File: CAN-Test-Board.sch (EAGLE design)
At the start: 47 parts, among them Y1 ECS-80-S-4X, Y2 ECS-80-S-4X

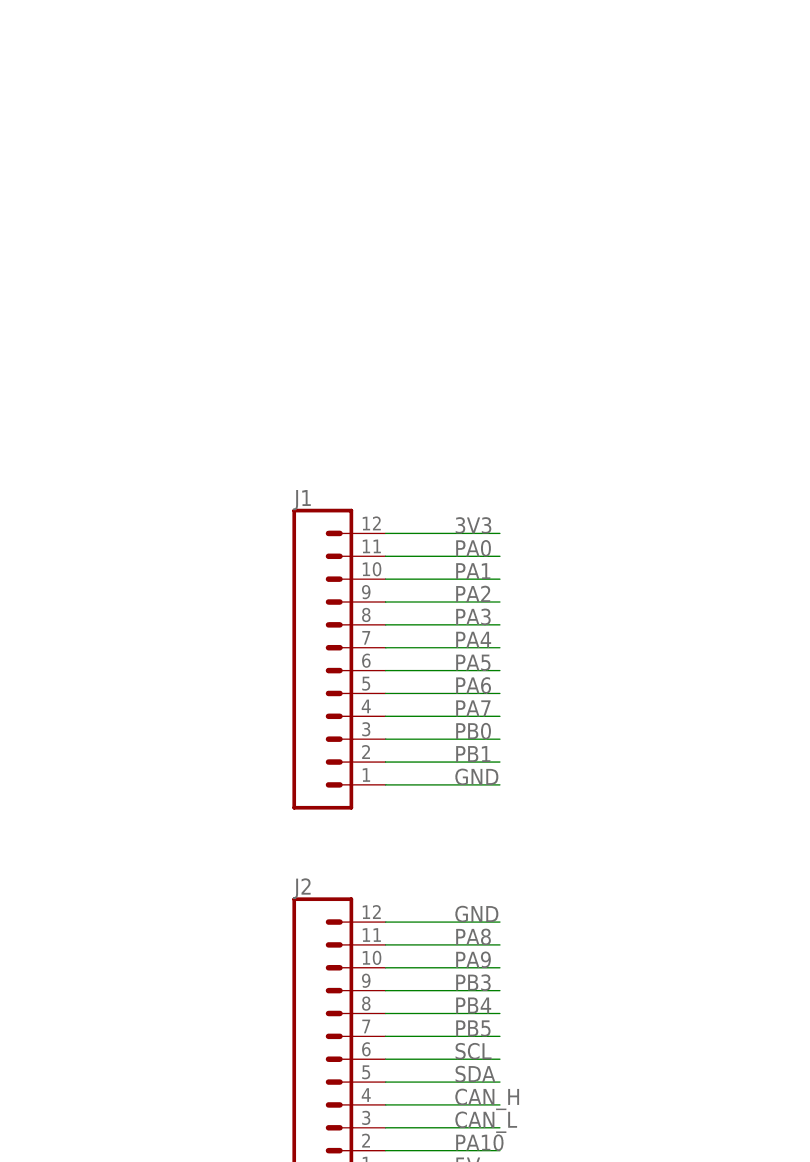
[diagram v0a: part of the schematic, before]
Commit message: smaller and extra CAN breakouts
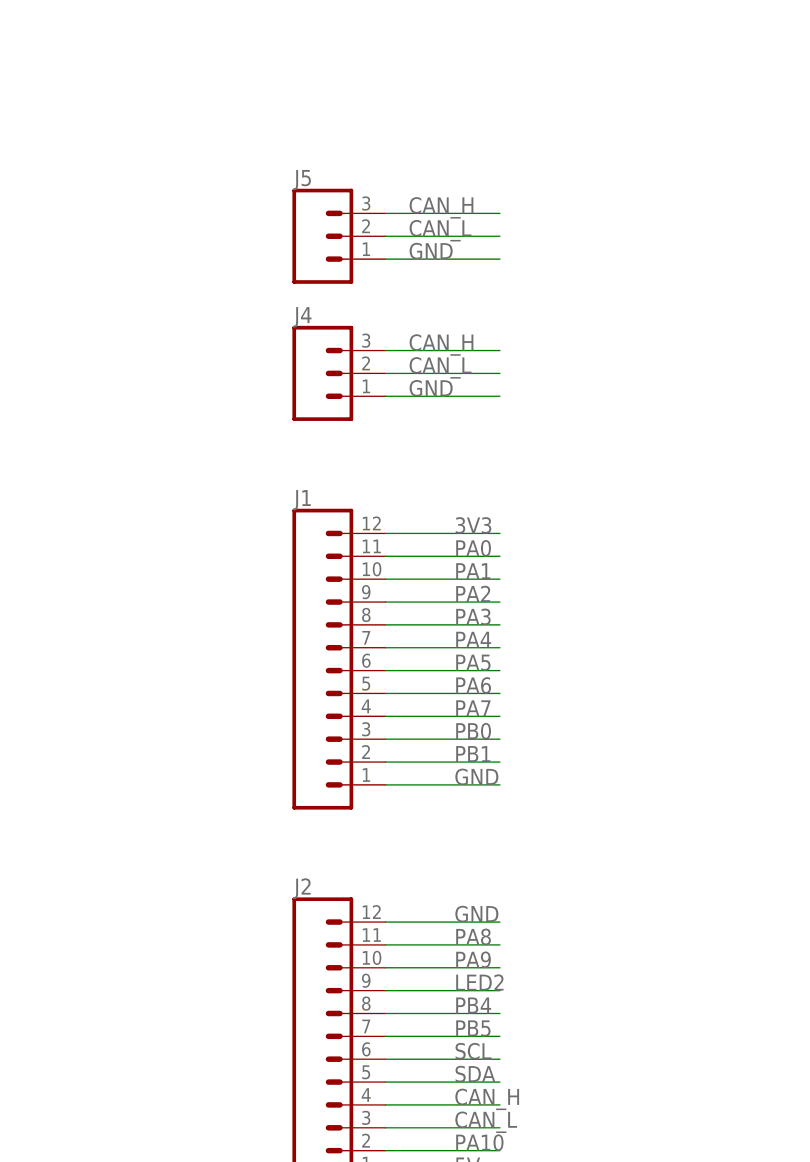
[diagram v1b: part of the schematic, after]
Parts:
- added J4, J5: (no value), SparkFun-Connectors:CONN_03
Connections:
- removed net PB3: J2.9
- net CAN_H: now also J4.3, J5.3
- net CAN_L: now also J4.2, J5.2
- net GND: now also J4.1, J5.1
- net LED2: now also J2.9
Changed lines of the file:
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@@
 <part name="R12" library="SparkFun-Resistors" library_urn="urn:adsk.eagle:library:532" deviceset="1KOHM" device="-0603-1/10W-1%" package3d_urn="urn:adsk.eagle:package:39650/1" value="10k"/>
 <part name="R13" library="SparkFun-Resistors" library_urn="urn:adsk.eagle:library:532" deviceset="1KOHM" device="-0603-1/10W-1%" package3d_urn="urn:adsk.eagle:package:39650/1" value="10k"/>
+<part name="J4" library="SparkFun-Connectors" library_urn="urn:adsk.eagle:library:513" deviceset="CONN_03" device="" package3d_urn="urn:adsk.eagle:package:38063/1"/>
+<part name="J5" library="SparkFun-Connectors" library_urn="urn:adsk.eagle:library:513" deviceset="CONN_03" device="" package3d_urn="urn:adsk.eagle:package:38063/1"/>
 </parts>
 <sheets>
@@
 <attribute name="NAME" x="135.636" y="165.1" size="1.778" layer="95" font="vector" rot="R90" align="bottom-center"/>
 <attribute name="VALUE" x="138.684" y="165.1" size="1.778" layer="96" font="vector" rot="R90" align="top-center"/>
+</instance>
+<instance part="J4" gate="J$1" x="307.34" y="116.84" smashed="yes">
+<attribute name="VALUE" x="304.8" y="109.474" size="1.778" layer="96" font="vector"/>
+<attribute name="NAME" x="304.8" y="122.428" size="1.778" layer="95" font="vector"/>
+</instance>
+<instance part="J5" gate="J$1" x="307.34" y="132.08" smashed="yes">
+<attribute name="VALUE" x="304.8" y="124.714" size="1.778" layer="96" font="vector"/>
+<attribute name="NAME" x="304.8" y="137.668" size="1.778" layer="95" font="vector"/>
 </instance>
 </instances>
@@
 <label x="322.58" y="55.88" size="1.778" layer="95"/>
 </segment>
+<segment>
+<pinref part="J4" gate="J$1" pin="1"/>
+<wire x1="314.96" y1="114.3" x2="327.66" y2="114.3" width="0.1524" layer="91"/>
+<label x="317.5" y="114.3" size="1.778" layer="95" rot="MR0" align="bottom-right"/>
+</segment>
+<segment>
+<pinref part="J5" gate="J$1" pin="1"/>
+<wire x1="314.96" y1="129.54" x2="327.66" y2="129.54" width="0.1524" layer="91"/>
+<label x="317.5" y="129.54" size="1.778" layer="95" rot="MR0" align="bottom-right"/>
+</segment>
 </net>
 <net name="CAN_H" class="1">
@@
 <pinref part="J2" gate="G$1" pin="4"/>
 <label x="322.58" y="35.56" size="1.778" layer="95"/>
+</segment>
+<segment>
+<pinref part="J4" gate="J$1" pin="3"/>
+<wire x1="314.96" y1="119.38" x2="327.66" y2="119.38" width="0.1524" layer="91"/>
+<label x="317.5" y="119.38" size="1.778" layer="95" rot="MR0" align="bottom-right"/>
+</segment>
+<segment>
+<pinref part="J5" gate="J$1" pin="3"/>
+<wire x1="314.96" y1="134.62" x2="327.66" y2="134.62" width="0.1524" layer="91"/>
+<label x="317.5" y="134.62" size="1.778" layer="95" rot="MR0" align="bottom-right"/>
 </segment>
 </net>
@@
 <pinref part="J2" gate="G$1" pin="3"/>
 <label x="322.58" y="33.02" size="1.778" layer="95"/>
+</segment>
+<segment>
+<pinref part="J4" gate="J$1" pin="2"/>
+<wire x1="314.96" y1="116.84" x2="327.66" y2="116.84" width="0.1524" layer="91"/>
+<label x="317.5" y="116.84" size="1.778" layer="95" rot="MR0" align="bottom-right"/>
+</segment>
+<segment>
+<pinref part="J5" gate="J$1" pin="2"/>
+<wire x1="314.96" y1="132.08" x2="327.66" y2="132.08" width="0.1524" layer="91"/>
+<label x="317.5" y="132.08" size="1.778" layer="95" rot="MR0" align="bottom-right"/>
 </segment>
 </net>
@@
 <label x="190.5" y="157.48" size="1.778" layer="95" rot="R90"/>
 </segment>
+<segment>
+<wire x1="314.96" y1="48.26" x2="327.66" y2="48.26" width="0.1524" layer="91"/>
+<pinref part="J2" gate="G$1" pin="9"/>
+<label x="322.58" y="48.26" size="1.778" layer="95"/>
+</segment>
 </net>
 <net name="SCLK" class="0">
@@
 <wire x1="157.48" y1="243.84" x2="139.7" y2="243.84" width="0.1524" layer="91"/>
 <label x="139.7" y="243.84" size="1.778" layer="95"/>
-</segment>
-</net>
-<net name="PB3" class="0">
-<segment>
-<wire x1="314.96" y1="48.26" x2="327.66" y2="48.26" width="0.1524" layer="91"/>
-<pinref part="J2" gate="G$1" pin="9"/>
-<label x="322.58" y="48.26" size="1.778" layer="95"/>
 </segment>
 </net>
@@
 packages will not be understood (or retained) with this version.
 </note>
+<note version="9.0" severity="warning">
+Since Version 9.0, EAGLE supports the align property for labels.
+Labels in schematic will not be understood with this version. Update EAGLE to the latest version
+for full support of labels.
+</note>
 <note version="8.5" severity="warning">

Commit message: labels and 3v3 power options
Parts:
- added R14: (no value), SparkFun-Resistors:RESISTOR0603
- added R15: 0, SparkFun-Resistors:RESISTOR0603
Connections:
- new net 3V3_PI: PCB1.3V3@1, PCB1.3V3@17, R15.1
- new net 3V3_REG: C17.1, R14.2, U$5.OUT
- net 3V3: now also R14.1, R15.2; no longer C17.1, U$5.OUT
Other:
- moved on the sheet: C17, C18
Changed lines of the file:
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@@
 <part name="J4" library="SparkFun-Connectors" library_urn="urn:adsk.eagle:library:513" deviceset="CONN_03" device="" package3d_urn="urn:adsk.eagle:package:38063/1"/>
 <part name="J5" library="SparkFun-Connectors" library_urn="urn:adsk.eagle:library:513" deviceset="CONN_03" device="" package3d_urn="urn:adsk.eagle:package:38063/1"/>
+<part name="R14" library="SparkFun-Resistors" library_urn="urn:adsk.eagle:library:532" deviceset="RESISTOR" device="0603" package3d_urn="urn:adsk.eagle:package:39650/1" value=" "/>
+<part name="R15" library="SparkFun-Resistors" library_urn="urn:adsk.eagle:library:532" deviceset="RESISTOR" device="0603" package3d_urn="urn:adsk.eagle:package:39650/1" value="0"/>
 </parts>
 <sheets>
@@
 <attribute name="SHEET" x="195.58" y="189.23" size="2.54" layer="94" font="vector"/>
 </instance>
-<instance part="U$5" gate="G$1" x="515.62" y="55.88" smashed="yes"/>
-<instance part="GND20" gate="1" x="523.24" y="35.56" smashed="yes">
-<attribute name="VALUE" x="523.24" y="35.306" size="1.778" layer="96" align="top-center"/>
-</instance>
-<instance part="C17" gate="G$1" x="538.48" y="43.18" smashed="yes">
-<attribute name="NAME" x="540.004" y="46.101" size="1.778" layer="95" font="vector"/>
-<attribute name="VALUE" x="540.004" y="41.021" size="1.778" layer="96" font="vector"/>
-</instance>
-<instance part="C18" gate="G$1" x="502.92" y="43.18" smashed="yes">
-<attribute name="NAME" x="504.444" y="46.101" size="1.778" layer="95" font="vector"/>
-<attribute name="VALUE" x="504.444" y="41.021" size="1.778" layer="96" font="vector"/>
-</instance>
-<instance part="GND21" gate="1" x="538.48" y="35.56" smashed="yes">
-<attribute name="VALUE" x="538.48" y="35.306" size="1.778" layer="96" align="top-center"/>
-</instance>
-<instance part="GND22" gate="1" x="502.92" y="35.56" smashed="yes">
-<attribute name="VALUE" x="502.92" y="35.306" size="1.778" layer="96" align="top-center"/>
+<instance part="U$5" gate="G$1" x="492.76" y="60.96" smashed="yes"/>
+<instance part="GND20" gate="1" x="500.38" y="40.64" smashed="yes">
+<attribute name="VALUE" x="500.38" y="40.386" size="1.778" layer="96" align="top-center"/>
+</instance>
+<instance part="C17" gate="G$1" x="515.62" y="48.26" smashed="yes">
+<attribute name="NAME" x="517.144" y="51.181" size="1.778" layer="95" font="vector"/>
+<attribute name="VALUE" x="517.144" y="46.101" size="1.778" layer="96" font="vector"/>
+</instance>
+<instance part="C18" gate="G$1" x="480.06" y="48.26" smashed="yes">
+<attribute name="NAME" x="481.584" y="51.181" size="1.778" layer="95" font="vector"/>
+<attribute name="VALUE" x="481.584" y="46.101" size="1.778" layer="96" font="vector"/>
+</instance>
+<instance part="GND21" gate="1" x="515.62" y="40.64" smashed="yes">
+<attribute name="VALUE" x="515.62" y="40.386" size="1.778" layer="96" align="top-center"/>
+</instance>
+<instance part="GND22" gate="1" x="480.06" y="40.64" smashed="yes">
+<attribute name="VALUE" x="480.06" y="40.386" size="1.778" layer="96" align="top-center"/>
 </instance>
 <instance part="D2" gate="G$1" x="220.98" y="35.56" smashed="yes">
@@
 <attribute name="VALUE" x="304.8" y="124.714" size="1.778" layer="96" font="vector"/>
 <attribute name="NAME" x="304.8" y="137.668" size="1.778" layer="95" font="vector"/>
+</instance>
+<instance part="R14" gate="G$1" x="525.78" y="55.88" smashed="yes" rot="R180">
+<attribute name="NAME" x="525.78" y="54.356" size="1.778" layer="95" font="vector" rot="R180" align="bottom-center"/>
+<attribute name="VALUE" x="525.78" y="57.404" size="1.778" layer="96" font="vector" rot="R180" align="top-center"/>
+</instance>
+<instance part="R15" gate="G$1" x="147.32" y="205.74" smashed="yes">
+<attribute name="NAME" x="147.32" y="207.264" size="1.778" layer="95" font="vector" align="bottom-center"/>
+<attribute name="VALUE" x="147.32" y="204.216" size="1.778" layer="96" font="vector" align="top-center"/>
 </instance>
 </instances>
@@
 <segment>
 <pinref part="U$5" gate="G$1" pin="GND"/>
-<wire x1="523.24" y1="40.64" x2="523.24" y2="38.1" width="0.1524" layer="91"/>
+<wire x1="500.38" y1="45.72" x2="500.38" y2="43.18" width="0.1524" layer="91"/>
 <pinref part="GND20" gate="1" pin="GND"/>
 </segment>
@@
 <pinref part="C18" gate="G$1" pin="2"/>
 <pinref part="GND22" gate="1" pin="GND"/>
-<wire x1="502.92" y1="40.64" x2="502.92" y2="38.1" width="0.1524" layer="91"/>
+<wire x1="480.06" y1="45.72" x2="480.06" y2="43.18" width="0.1524" layer="91"/>
 </segment>
 <segment>
 <pinref part="C17" gate="G$1" pin="2"/>
 <pinref part="GND21" gate="1" pin="GND"/>
-<wire x1="538.48" y1="40.64" x2="538.48" y2="38.1" width="0.1524" layer="91"/>
+<wire x1="515.62" y1="45.72" x2="515.62" y2="43.18" width="0.1524" layer="91"/>
 </segment>
 <segment>
@@
 <wire x1="198.12" y1="266.7" x2="198.12" y2="269.24" width="0.1524" layer="91"/>
 <label x="195.58" y="269.24" size="1.778" layer="95"/>
-</segment>
-<segment>
-<pinref part="U$5" gate="G$1" pin="OUT"/>
-<wire x1="535.94" y1="50.8" x2="538.48" y2="50.8" width="0.1524" layer="91"/>
-<label x="541.02" y="50.8" size="1.778" layer="95"/>
-<pinref part="C17" gate="G$1" pin="1"/>
-<wire x1="538.48" y1="50.8" x2="543.56" y2="50.8" width="0.1524" layer="91"/>
-<wire x1="538.48" y1="48.26" x2="538.48" y2="50.8" width="0.1524" layer="91"/>
-<junction x="538.48" y="50.8"/>
 </segment>
 <segment>
@@
 <label x="132.08" y="175.26" size="1.778" layer="95"/>
 </segment>
+<segment>
+<pinref part="R14" gate="G$1" pin="1"/>
+<wire x1="530.86" y1="55.88" x2="538.48" y2="55.88" width="0.1524" layer="91"/>
+<label x="533.4" y="55.88" size="1.778" layer="95"/>
+</segment>
+<segment>
+<pinref part="R15" gate="G$1" pin="2"/>
+<wire x1="152.4" y1="205.74" x2="165.1" y2="205.74" width="0.1524" layer="91"/>
+<label x="157.48" y="205.74" size="1.778" layer="95"/>
+</segment>
 </net>
 <net name="N$3" class="0">
@@
 <segment>
 <pinref part="U$5" gate="G$1" pin="VDD"/>
-<wire x1="510.54" y1="53.34" x2="508" y2="53.34" width="0.1524" layer="91"/>
-<label x="502.92" y="53.34" size="1.778" layer="95"/>
+<wire x1="487.68" y1="58.42" x2="485.14" y2="58.42" width="0.1524" layer="91"/>
+<label x="480.06" y="58.42" size="1.778" layer="95"/>
 <pinref part="U$5" gate="G$1" pin="EN"/>
-<wire x1="508" y1="53.34" x2="502.92" y2="53.34" width="0.1524" layer="91"/>
-<wire x1="510.54" y1="48.26" x2="508" y2="48.26" width="0.1524" layer="91"/>
-<wire x1="508" y1="48.26" x2="508" y2="53.34" width="0.1524" layer="91"/>
-<junction x="508" y="53.34"/>
-<wire x1="502.92" y1="53.34" x2="500.38" y2="53.34" width="0.1524" layer="91"/>
+<wire x1="485.14" y1="58.42" x2="480.06" y2="58.42" width="0.1524" layer="91"/>
+<wire x1="487.68" y1="53.34" x2="485.14" y2="53.34" width="0.1524" layer="91"/>
+<wire x1="485.14" y1="53.34" x2="485.14" y2="58.42" width="0.1524" layer="91"/>
+<junction x="485.14" y="58.42"/>
+<wire x1="480.06" y1="58.42" x2="477.52" y2="58.42" width="0.1524" layer="91"/>
 <pinref part="C18" gate="G$1" pin="1"/>
-<wire x1="502.92" y1="48.26" x2="502.92" y2="53.34" width="0.1524" layer="91"/>
-<junction x="502.92" y="53.34"/>
+<wire x1="480.06" y1="53.34" x2="480.06" y2="58.42" width="0.1524" layer="91"/>
+<junction x="480.06" y="58.42"/>
 </segment>
 <segment>
@@
 </segment>
 </net>
+<net name="3V3_REG" class="2">
+<segment>
+<pinref part="U$5" gate="G$1" pin="OUT"/>
+<wire x1="513.08" y1="55.88" x2="515.62" y2="55.88" width="0.1524" layer="91"/>
+<label x="513.08" y="55.88" size="1.778" layer="95"/>
+<pinref part="C17" gate="G$1" pin="1"/>
+<wire x1="515.62" y1="55.88" x2="520.7" y2="55.88" width="0.1524" layer="91"/>
+<wire x1="515.62" y1="53.34" x2="515.62" y2="55.88" width="0.1524" layer="91"/>
+<junction x="515.62" y="55.88"/>
+<pinref part="R14" gate="G$1" pin="2"/>
+</segment>
+</net>
+<net name="3V3_PI" class="2">
+<segment>
+<pinref part="PCB1" gate="G$1" pin="3V3@17"/>
+<wire x1="48.26" y1="246.38" x2="58.42" y2="246.38" width="0.1524" layer="91"/>
+<label x="53.34" y="246.38" size="1.778" layer="95"/>
+</segment>
+<segment>
+<pinref part="PCB1" gate="G$1" pin="3V3@1"/>
+<wire x1="48.26" y1="205.74" x2="58.42" y2="205.74" width="0.1524" layer="91"/>
+<label x="53.34" y="205.74" size="1.778" layer="95"/>
+</segment>
+<segment>
+<pinref part="R15" gate="G$1" pin="1"/>
+<wire x1="142.24" y1="205.74" x2="132.08" y2="205.74" width="0.1524" layer="91"/>
+<label x="132.08" y="205.74" size="1.778" layer="95"/>
+</segment>
+</net>

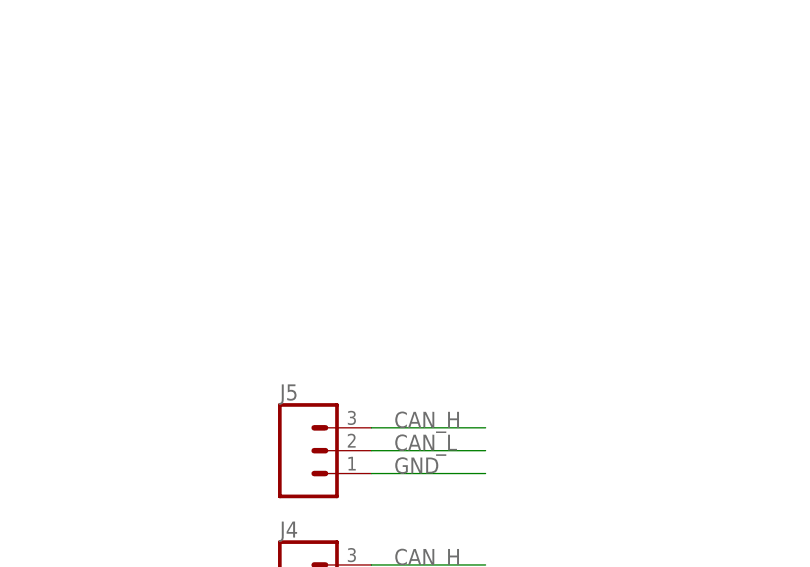
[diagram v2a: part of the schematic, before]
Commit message: added samtec t2i
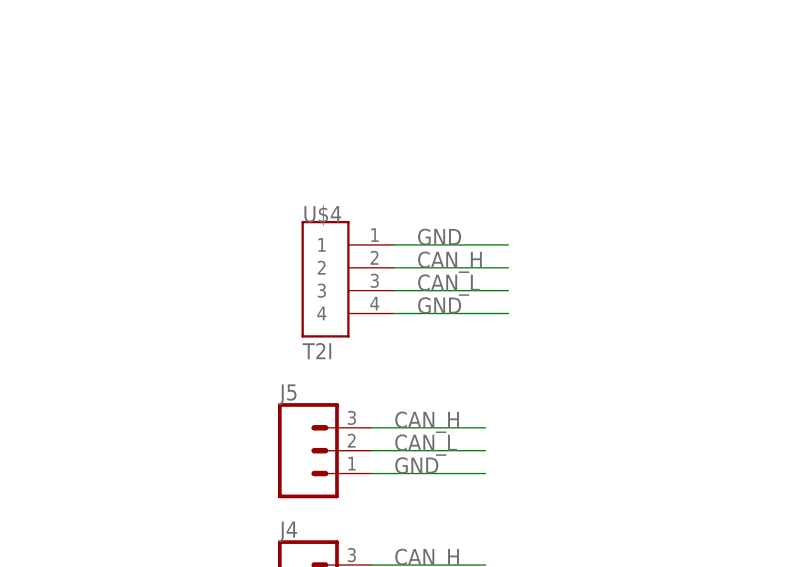
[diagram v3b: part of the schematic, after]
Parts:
- added U$4: T2I, Samtec t2i:T2I
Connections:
- net CAN_H: now also U$4.2
- net CAN_L: now also U$4.3
- net GND: now also U$4.1, U$4.4
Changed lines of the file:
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@@
 <part name="R14" library="SparkFun-Resistors" library_urn="urn:adsk.eagle:library:532" deviceset="RESISTOR" device="0603" package3d_urn="urn:adsk.eagle:package:39650/1" value=" "/>
 <part name="R15" library="SparkFun-Resistors" library_urn="urn:adsk.eagle:library:532" deviceset="RESISTOR" device="0603" package3d_urn="urn:adsk.eagle:package:39650/1" value="0"/>
+<part name="U$4" library="Samtec t2i" deviceset="T2I" device="" package3d_urn="urn:adsk.eagle:package:23194708/2"/>
 </parts>
 <sheets>
@@
 <attribute name="NAME" x="147.32" y="207.264" size="1.778" layer="95" font="vector" align="bottom-center"/>
 <attribute name="VALUE" x="147.32" y="204.216" size="1.778" layer="96" font="vector" align="top-center"/>
+</instance>
+<instance part="U$4" gate="G$1" x="309.88" y="154.94" smashed="yes">
+<attribute name="NAME" x="307.34" y="157.48" size="1.778" layer="95"/>
+<attribute name="VALUE" x="307.34" y="142.24" size="1.778" layer="96"/>
 </instance>
 </instances>
@@
 <label x="317.5" y="129.54" size="1.778" layer="95" rot="MR0" align="bottom-right"/>
 </segment>
+<segment>
+<wire x1="317.5" y1="147.32" x2="330.2" y2="147.32" width="0.1524" layer="91"/>
+<label x="320.04" y="147.32" size="1.778" layer="95" rot="MR0" align="bottom-right"/>
+<pinref part="U$4" gate="G$1" pin="4"/>
+</segment>
+<segment>
+<wire x1="317.5" y1="154.94" x2="330.2" y2="154.94" width="0.1524" layer="91"/>
+<pinref part="U$4" gate="G$1" pin="1"/>
+<label x="320.04" y="154.94" size="1.778" layer="95"/>
+</segment>
 </net>
 <net name="CAN_H" class="1">
@@
 <wire x1="314.96" y1="134.62" x2="327.66" y2="134.62" width="0.1524" layer="91"/>
 <label x="317.5" y="134.62" size="1.778" layer="95" rot="MR0" align="bottom-right"/>
+</segment>
+<segment>
+<wire x1="317.5" y1="152.4" x2="330.2" y2="152.4" width="0.1524" layer="91"/>
+<label x="320.04" y="152.4" size="1.778" layer="95" rot="MR0" align="bottom-right"/>
+<pinref part="U$4" gate="G$1" pin="2"/>
 </segment>
 </net>
@@
 <label x="317.5" y="132.08" size="1.778" layer="95" rot="MR0" align="bottom-right"/>
 </segment>
+<segment>
+<wire x1="317.5" y1="149.86" x2="330.2" y2="149.86" width="0.1524" layer="91"/>
+<label x="320.04" y="149.86" size="1.778" layer="95" rot="MR0" align="bottom-right"/>
+<pinref part="U$4" gate="G$1" pin="3"/>
+</segment>
 </net>
